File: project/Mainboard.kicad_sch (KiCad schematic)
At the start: 0 parts

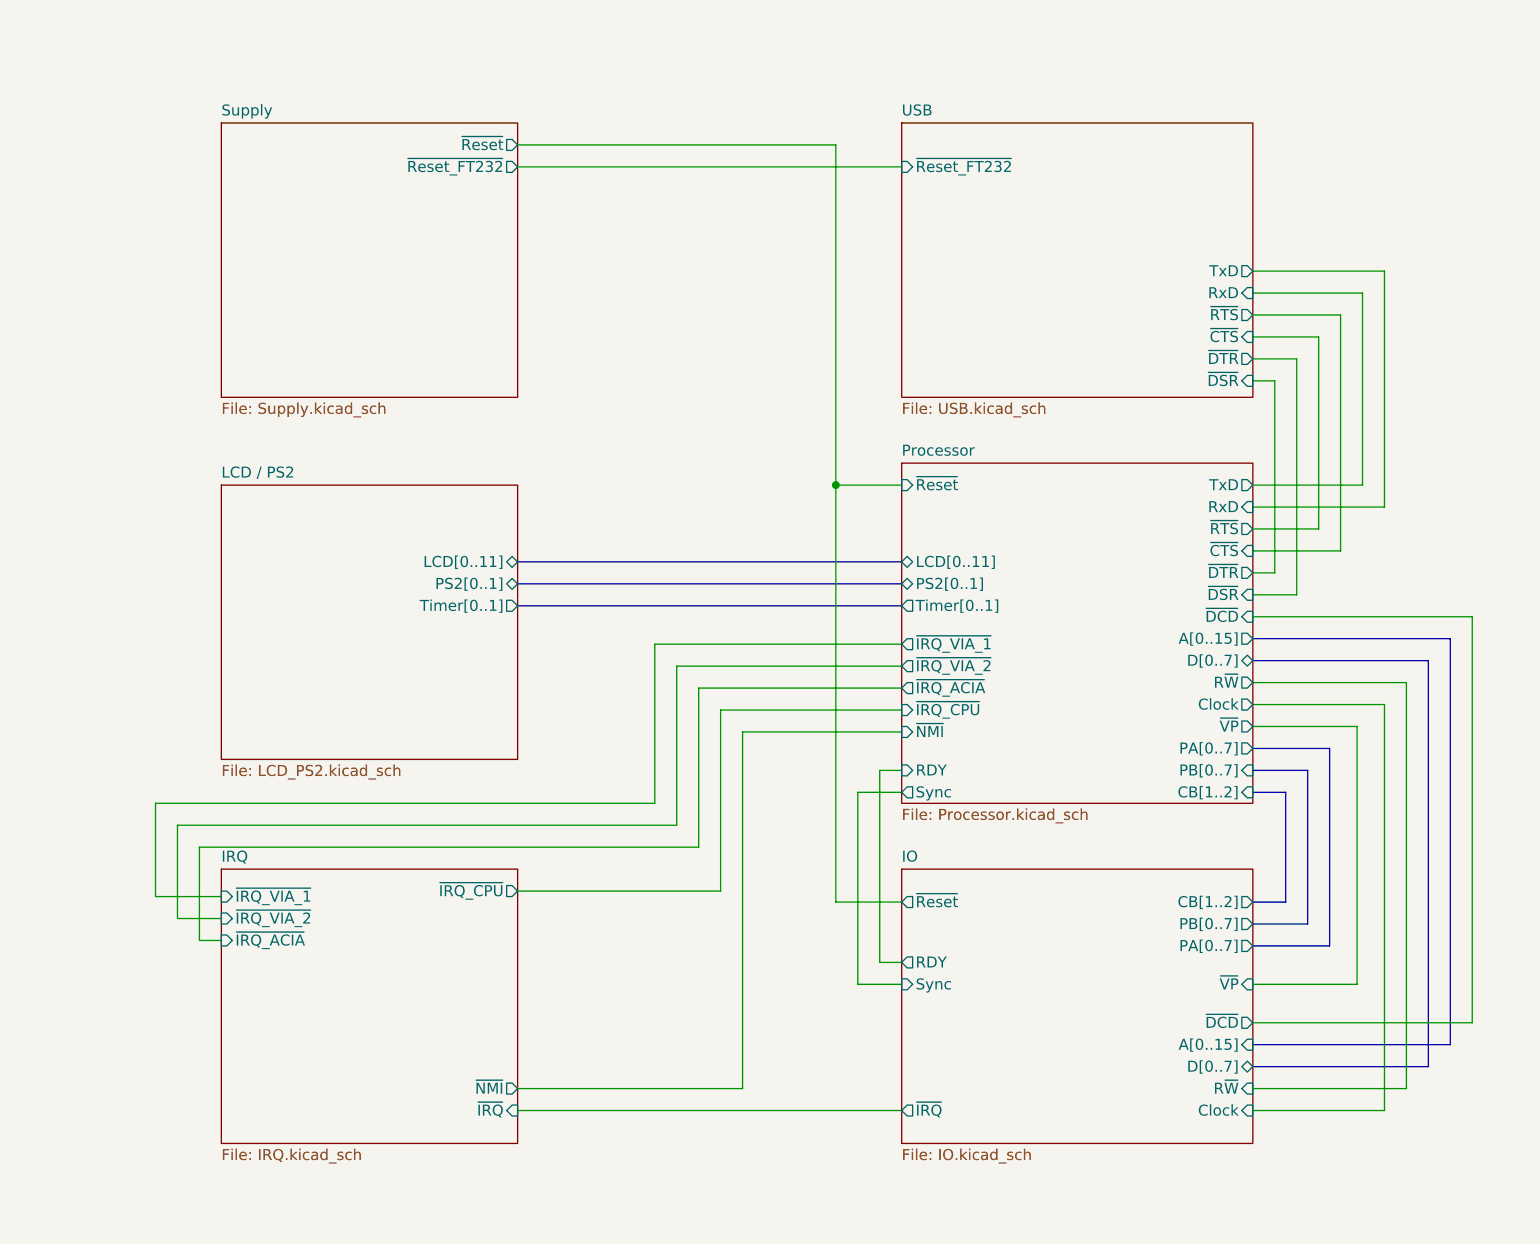
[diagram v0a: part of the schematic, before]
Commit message: Fix grid issues, fix missing libraries, replace FT232 with FT231
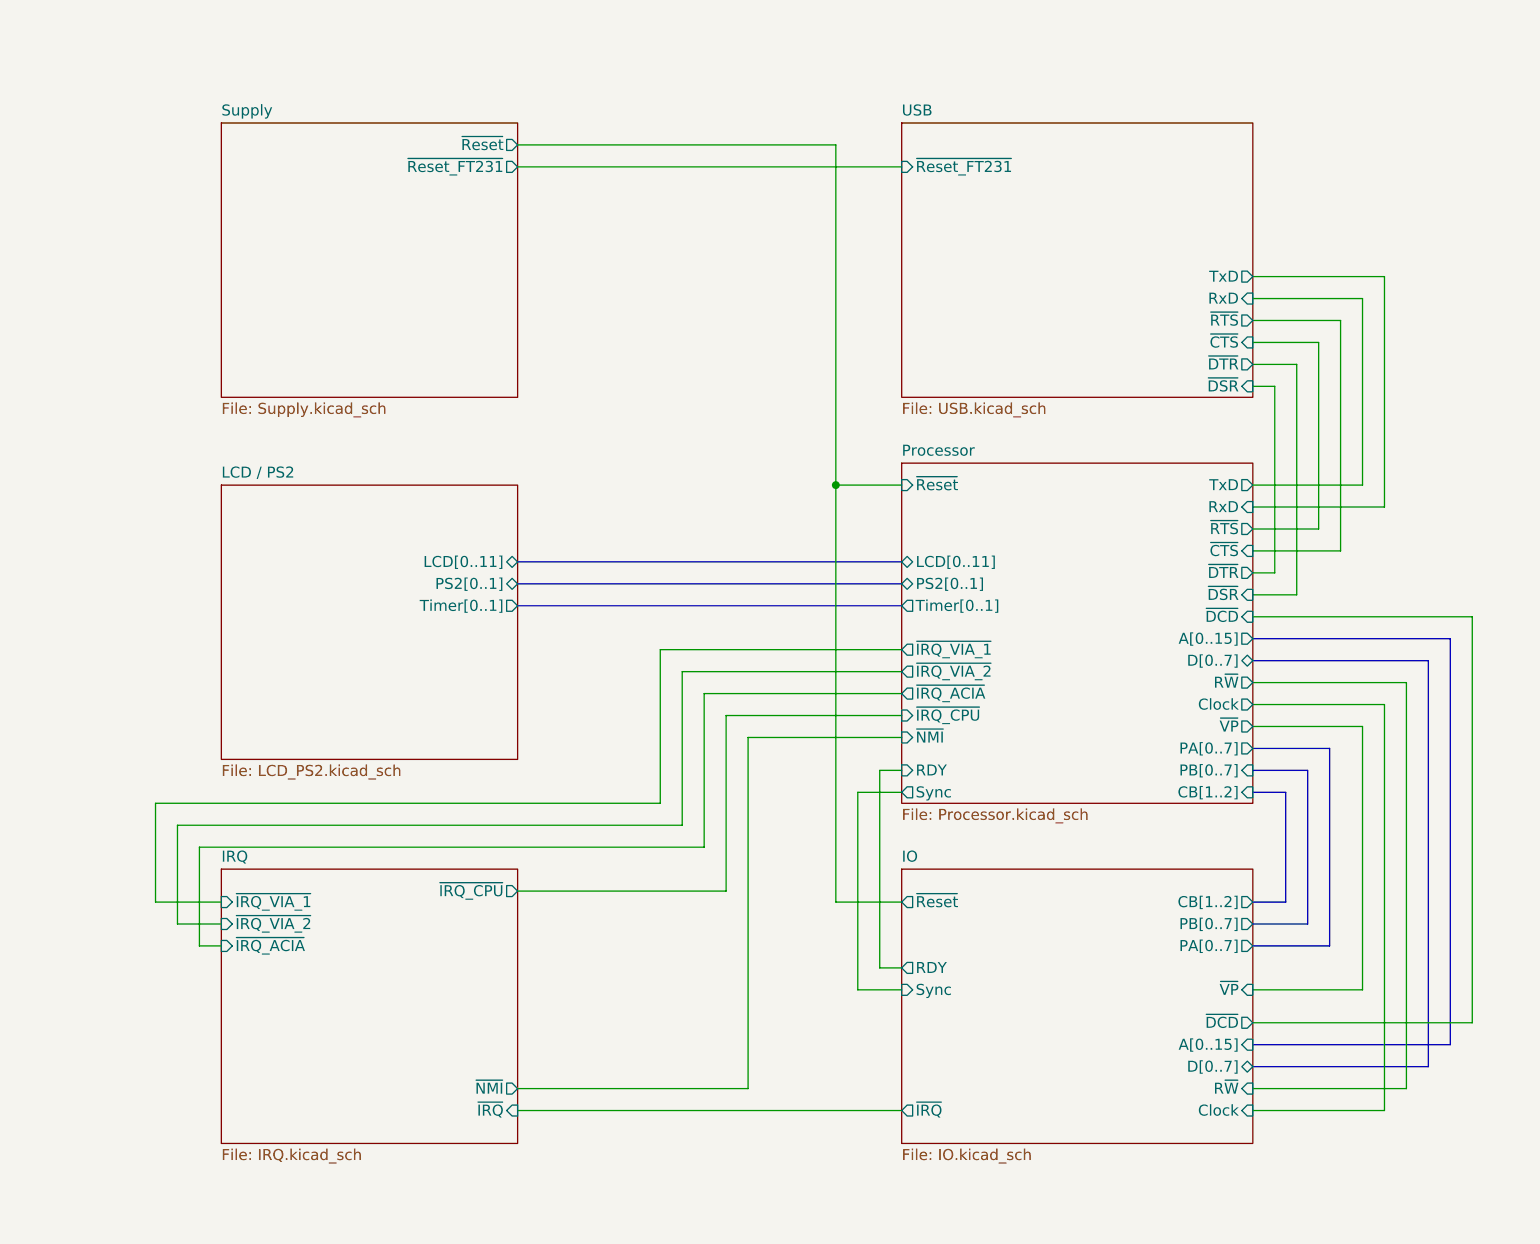
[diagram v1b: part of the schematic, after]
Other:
- sheet Supply ports: added ~{Reset_FT231}; removed ~{Reset_FT232}
- sheet USB ports: added ~{Reset_FT231}; removed ~{Reset_FT232}
